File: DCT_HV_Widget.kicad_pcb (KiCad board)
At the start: 2 copper layers, 88.9 x 88.9 mm, 23 parts, among them J1 Control Voltage, J2 Bench Power Supply, J3 High Voltage, Q1 ZXTN10150D, U1 LT1468CS8-PBF, U2 OC150G

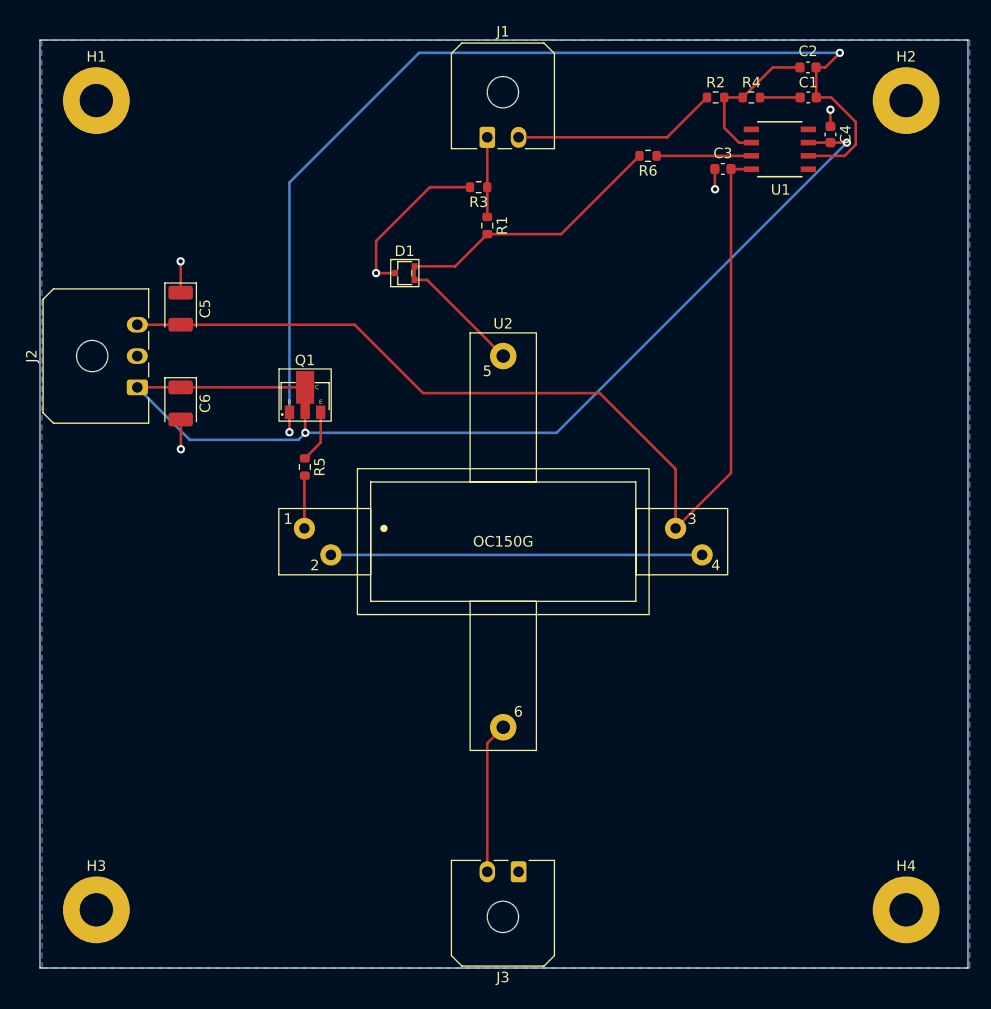
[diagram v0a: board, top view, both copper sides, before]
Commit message: Updated PCB with Gerard feedback
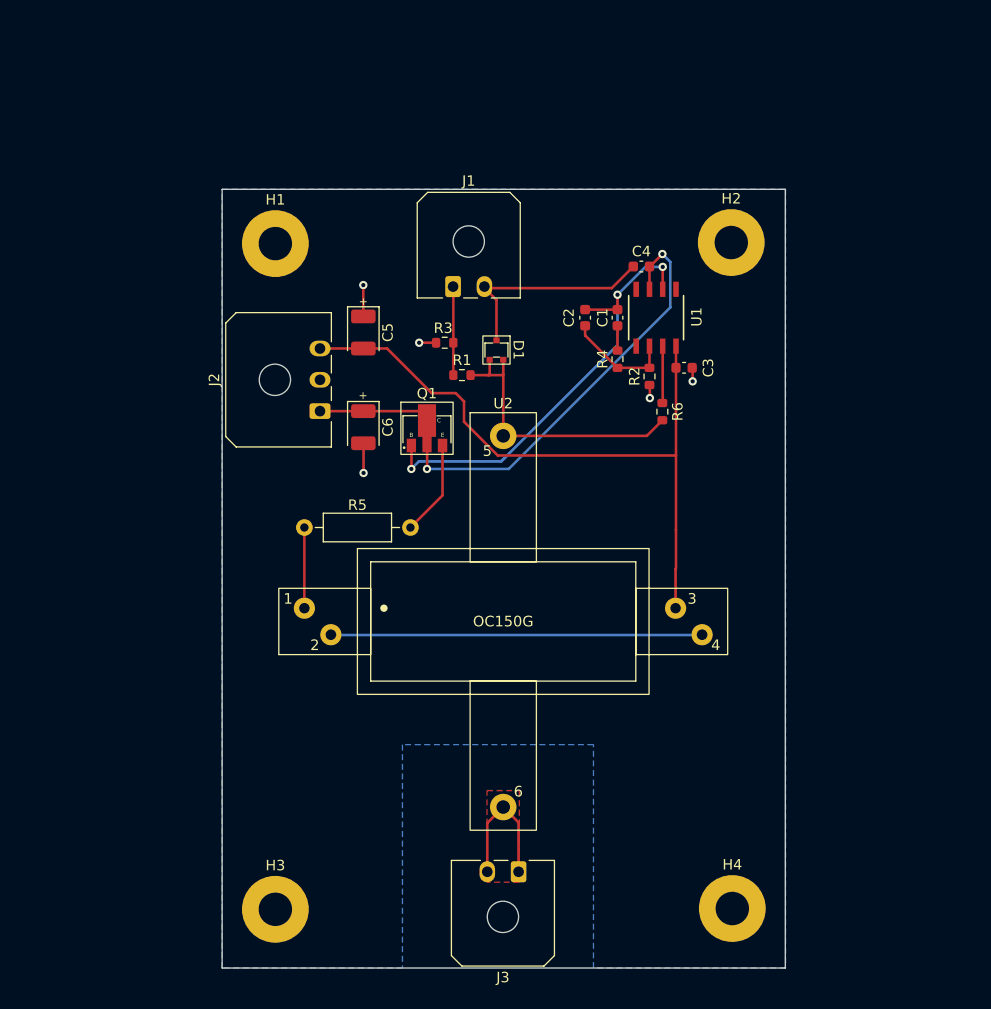
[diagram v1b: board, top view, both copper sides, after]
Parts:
- R5: footprint Resistor_SMD:R_0603_1608Metric -> Resistor_THT:R_Axial_DIN0207_L6.3mm_D2.5mm_P10.16mm_Horizontal
- moved C2 32.1 mm to (168.2, 81.7), turned to 90 degrees
- moved R4 28.2 mm to (171.3, 85.7), turned to 90 degrees
- moved C1 27.9 mm to (171.3, 81.7), turned to 90 degrees
- moved R2 27.5 mm to (174.4, 87.3), turned to 90 degrees
- moved R6 24.5 mm to (175.6, 90.7), turned to -90 degrees
- moved C4 22.1 mm to (173.6, 76.8), turned to 180 degrees
- moved H1 22.0 mm to (138.5, 74.6)
- moved H2 21.6 mm to (182.2, 74.5)
- moved U1 20.0 mm to (175.0, 81.7), turned to 90 degrees
- moved C3 19.4 mm to (177.7, 86.5), turned to 180 degrees
- moved J2 17.6 mm to (142.8, 90.7)
- moved C5 17.6 mm to (146.9, 83.1)
- moved C6 17.6 mm to (146.9, 92.2)
- moved H3 17.2 mm to (138.5, 138.4)
- moved H4 16.7 mm to (182.3, 138.3)
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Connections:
- J3 pad 1: GND -> /HV_Input
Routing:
- net Net-(C1-Pad2): track 101.4 -> 44.5 mm, vias 2 -> 3
- net /VP6: track 103.0 -> 52.2 mm
- net /VM6: track 101.6 -> 64.6 mm
- net GND: track 45.2 -> 30.8 mm
- net Net-(D1-Pad1): track 38.8 -> 27.8 mm
- net Net-(Q1-Pad1): track 5.04 -> 9.13 mm
- net Net-(C2-Pad1): track 14.5 -> 10.4 mm
- net Net-(R6-Pad1): track 9.08 -> 5.47 mm
- net Net-(R5-Pad2): track 5.08 -> 7.73 mm
- net Net-(C1-Pad1): track 3.85 -> 2.38 mm
- net /HV_Input: track 14.5 -> 13.6 mm
- net /V_Control: track 7.63 -> 8.33 mm
- added copper zone on F.Cu, net /HV_Input
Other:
- board size 88.9 x 88.9 mm -> 53.9 x 74.6 mm
- board text added: "+"

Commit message: Updated PCB with silkscreens
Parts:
- added G***: LOGO, LOGO, F.Cu at (177.7, 99.7)
- added G***: LOGO, LOGO, F.Cu at (145.3, 125.7)
- added G***: LOGO, LOGO, F.Cu at (178.6, 126.0)
- added G***: LOGO, LOGO, B.Cu at (163.6, 109.4)
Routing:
- net GND: track 30.8 -> 17.0 mm, vias 5 -> 6
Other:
- board text added: "Bench Power"
- board text added: "Control"
- board text added: "Dennis H. Calderon 02/28/2023"
- board text added: "FLoBBr"
- board text added: "Fantastic Load Bearing Board (FLoBBr)"
- board text added: "High Voltage"

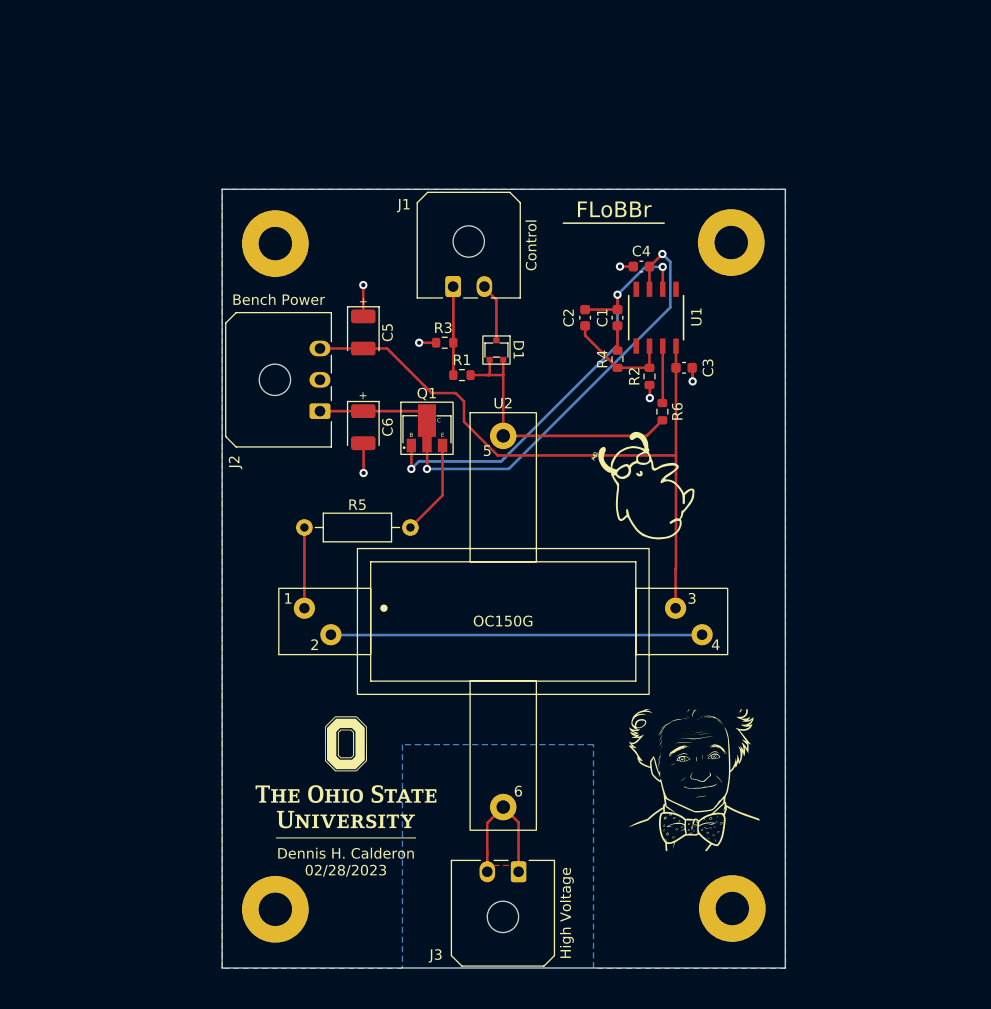
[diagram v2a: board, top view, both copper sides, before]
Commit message: Updated PCB. Increased HV clearance. Added 0.6mm solder expansion. C2 closer to R4. Increased size of pin 1 marking for U1.
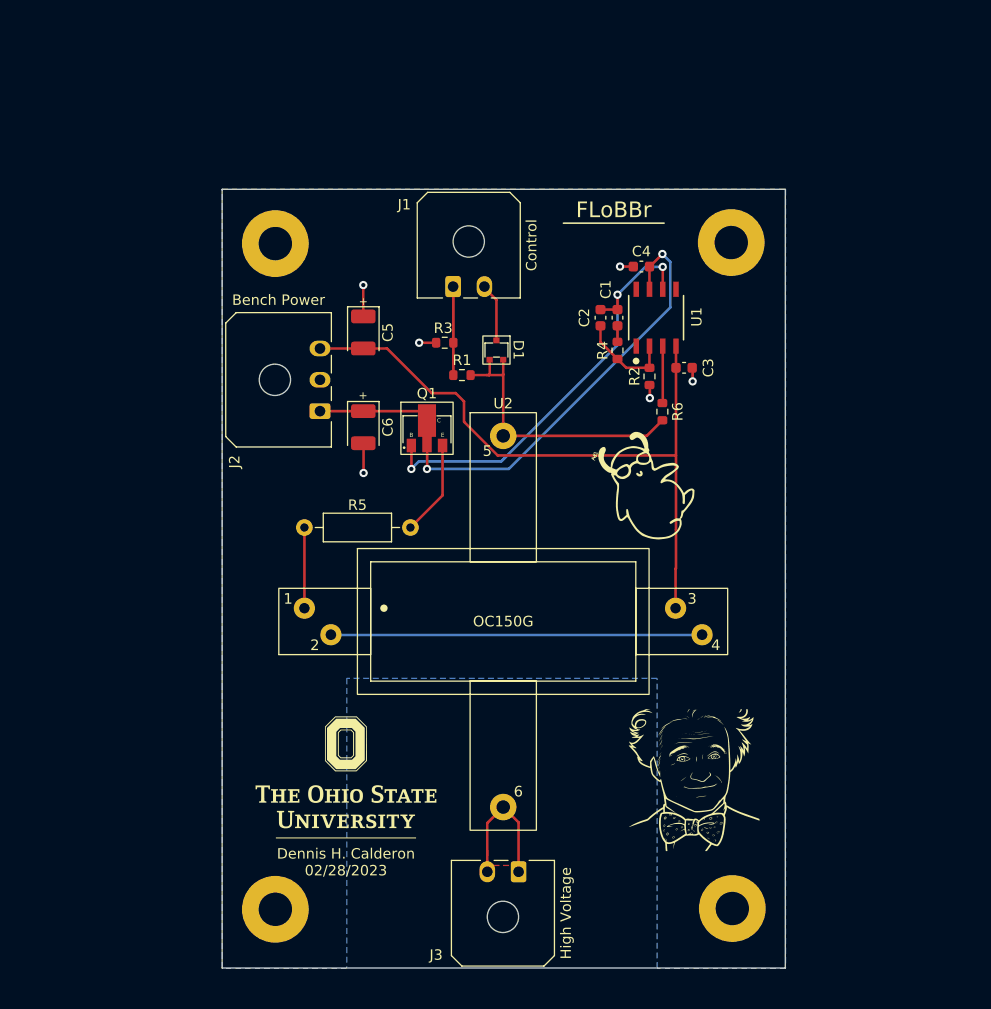
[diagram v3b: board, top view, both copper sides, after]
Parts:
- moved C2 1.47 mm to (169.7, 81.7)
- moved R4 0.84 mm to (171.3, 84.8)
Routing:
- net Net-(C1-Pad2): track 44.5 -> 43.0 mm
- net Net-(C2-Pad1): track 10.4 -> 9.35 mm
- net Net-(C1-Pad1): track 2.38 -> 1.54 mm
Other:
- rule pad_to_mask_clearance: 0 -> 0.06
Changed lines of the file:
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@@
       (dielectric_constraints no)
     )
-    (pad_to_mask_clearance 0)
+    (pad_to_mask_clearance 0.06)
     (pcbplotparams
       (layerselection 0x00010fc_ffffffff)
@@
   )
   (footprint "Resistor_SMD:R_0603_1608Metric" (layer "F.Cu")
-    (at 171.3 85.675 90)
+    (at 171.3 84.836 90)
     (descr "Resistor SMD 0603 (1608 Metric), square (rectangular) end terminal, IPC_7351 nominal, (Body size source: IPC-SM-782 page 72, https://www.pcb-3d.com/wordpress/wp-content/uploads/ipc-sm-782a_amendment_1_and_2.pdf), generated with kicad-footprint-generator")
     (tags "resistor")
@@
     (property "Sheetname" "")
     (attr smd)
-    (fp_text reference "C1" (at 0 -1.43 90) (layer "F.SilkS")
+    (fp_text reference "C1" (at 2.706 -1.12 90) (layer "F.SilkS")
       (effects (font (size 1 1) (thickness 0.15)))
     )
@@
   )
   (footprint "Capacitor_SMD:C_0603_1608Metric" (layer "F.Cu")
-    (at 168.2 81.7 90)
+    (at 169.672 81.7 90)
     (descr "Capacitor SMD 0603 (1608 Metric), square (rectangular) end terminal, IPC_7351 nominal, (Body size source: IPC-SM-782 page 76, https://www.pcb-3d.com/wordpress/wp-content/uploads/ipc-sm-782a_amendment_1_and_2.pdf), generated with kicad-footprint-generator")
     (tags "capacitor")
@@
       ) (layer "B.SilkS") (width 0) (fill solid))
   )
-  (gr_circle (center 173.08 85.6) (end 173.08 85.6) (layer "F.SilkS") (width 0.15) (fill none))
+  (gr_circle (center 173.08 85.852) (end 173.33 85.852) (layer "F.SilkS") (width 0.15) (fill solid))
   (gr_line (start 166.116 72.644) (end 175.768 72.644) (layer "F.SilkS") (width 0.15))
   (gr_rect (start 133.425 69.4) (end 187.375 144) (layer "Edge.Cuts") (width 0.1016) (fill none))
@@
     (effects (font (size 1.5 1.5) (thickness 0.3)))
   )
-  (segment (start 171.3 84.85) (end 171.3 82.475) (width 0.25) (layer "F.Cu") (net 1))
+  (dimension (type aligned) (layer "Dwgs.User")
+    (pts (xy 160.274 128.778) (xy 160.355 116.515))
+    (height 0.762)
+    (gr_text "12.2633 mm" (at 159.276522 122.639644 89.6215534) (layer "Dwgs.User")
+      (effects (font (size 1.5 1.5) (thickness 0.3)))
+    )
+    (format (units 3) (units_format 1) (precision 4))
+    (style (thickness 0.2) (arrow_length 1.27) (text_position_mode 0) (extension_height 0.58642) (extension_offset 0.5) keep_text_aligned)
+  )
+  (dimension (type aligned) (layer "Dwgs.User")
+    (pts (xy 175.077 135.463) (xy 162.814 135.382))
+    (height 0.762)
+    (gr_text "12.2633 mm" (at 168.962422 132.860556 -0.3784465994) (layer "Dwgs.User")
+      (effects (font (size 1.5 1.5) (thickness 0.3)))
+    )
+    (format (units 3) (units_format 1) (precision 4))
+    (style (thickness 0.2) (arrow_length 1.27) (text_position_mode 0) (extension_height 0.58642) (extension_offset 0.5) keep_text_aligned)
+  )
+  (dimension (type aligned) (layer "Dwgs.User")
+    (pts (xy 157.805 135.717) (xy 145.542 135.636))
+    (height 0.762)
+    (gr_text "12.2633 mm" (at 151.690422 133.114556 -0.3784465994) (layer "Dwgs.User")
+      (effects (font (size 1.5 1.5) (thickness 0.3)))
+    )
+    (format (units 3) (units_format 1) (precision 4))
+    (style (thickness 0.2) (arrow_length 1.27) (text_position_mode 0) (extension_height 0.58642) (extension_offset 0.5) keep_text_aligned)
+  )
+  (segment (start 171.3 84.011) (end 171.3 82.475) (width 0.25) (layer "F.Cu") (net 1))
   (segment (start 151.565 93.9275) (end 151.565 96.1725) (width 0.25) (layer "F.Cu") (net 2))
-  (segment (start 171.3 80.925) (end 168.2 80.925) (width 0.25) (layer "F.Cu") (net 2))
+  (segment (start 171.3 80.925) (end 169.672 80.925) (width 0.25) (layer "F.Cu") (net 2))
   (segment (start 171.3 80.925) (end 171.3 79.5) (width 0.25) (layer "F.Cu") (net 2))
   (segment (start 175.635 78.97585) (end 175.635 76.835) (width 0.25) (layer "F.Cu") (net 2))
@@
   (segment (start 160.205671 95.425) (end 160.652835 94.977835) (width 0.25) (layer "B.Cu") (net 2))
   (segment (start 174.365 86.5) (end 174.365 84.42415) (width 0.25) (layer "F.Cu") (net 3))
-  (segment (start 168.2 83.4) (end 171.3 86.5) (width 0.25) (layer "F.Cu") (net 3))
-  (segment (start 171.3 86.5) (end 174.365 86.5) (width 0.25) (layer "F.Cu") (net 3))
-  (segment (start 168.2 82.475) (end 168.2 83.4) (width 0.25) (layer "F.Cu") (net 3))
+  (segment (start 169.672 82.475) (end 169.672 84.033) (width 0.25) (layer "F.Cu") (net 3))
+  (segment (start 169.672 84.033) (end 171.3 85.661) (width 0.25) (layer "F.Cu") (net 3))
+  (segment (start 172.139 86.5) (end 174.365 86.5) (width 0.25) (layer "F.Cu") (net 3))
+  (segment (start 171.3 85.661) (end 172.139 86.5) (width 0.25) (layer "F.Cu") (net 3))
   (segment (start 174.4 89.4) (end 174.4 88.185) (width 0.25) (layer "F.Cu") (net 4))
   (segment (start 178.5 86.545) (end 178.455 86.5) (width 0.25) (layer "F.Cu") (net 4))
@@
       (pts
         (xy 187.4 144)
-        (xy 169 144)
-        (xy 169 122.6)
-        (xy 150.7 122.6)
-        (xy 150.7 144)
+        (xy 175.096 144)
+        (xy 175.096 116.25)
+        (xy 145.366 116.25)
+        (xy 145.366 144)
         (xy 133.425 144)
         (xy 133.425 69.4)
@@
     )
   )
-  (group "" (id 2b9121dd-ebe4-4e7b-9878-c23b3f814f1b)
-    (members
-      12feab49-3c61-42f3-91d7-c7834095a1e1
-      1d146411-ecf5-4774-b910-fb684f881c87
-      5b9461f4-a323-4576-aed0-adc941585206
-      73c8fad7-f0f4-47e5-8556-11a945c789f9
-      ccf9a003-b1aa-4bea-8da9-f2a7e42de167
-      d2d1a73c-4bb2-44ed-bd20-7432b424a8ed
-      df63d8f9-e1ad-4a7a-9c86-2e7cba34b296
-      ef2e5de7-317e-431f-a79a-d954f6cb3478
-    )
-  )
